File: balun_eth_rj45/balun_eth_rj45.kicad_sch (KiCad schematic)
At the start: 17 parts, among them J1 RJE591885401 CAT6 NO-MAGNETICS, J2 SMA_A, J3 SMA_B, J4 SMA_C, J5 SMA_D, T1 ADT2-1T+, T2 ADT2-1T+, T3 ADT2-1T+, T4 ADT2-1T+

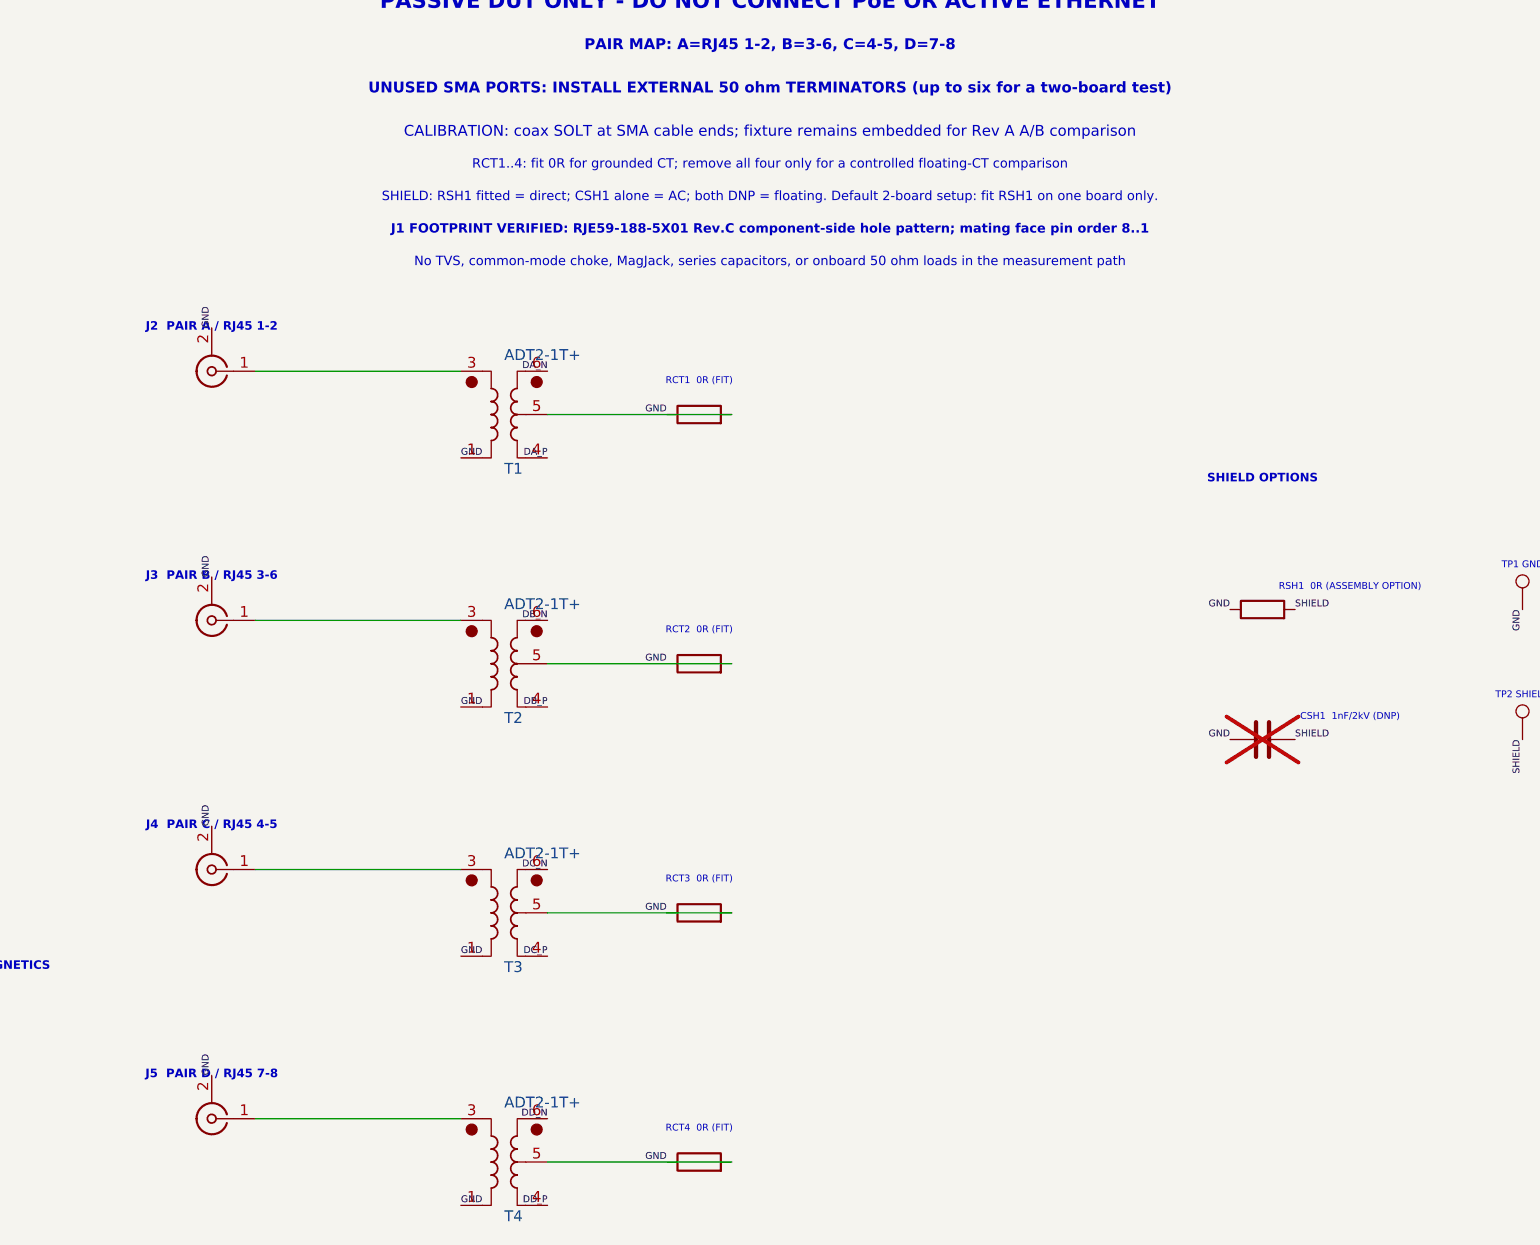
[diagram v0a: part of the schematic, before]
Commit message: feat: finalize slip-ring fixtures and floating CT baseline
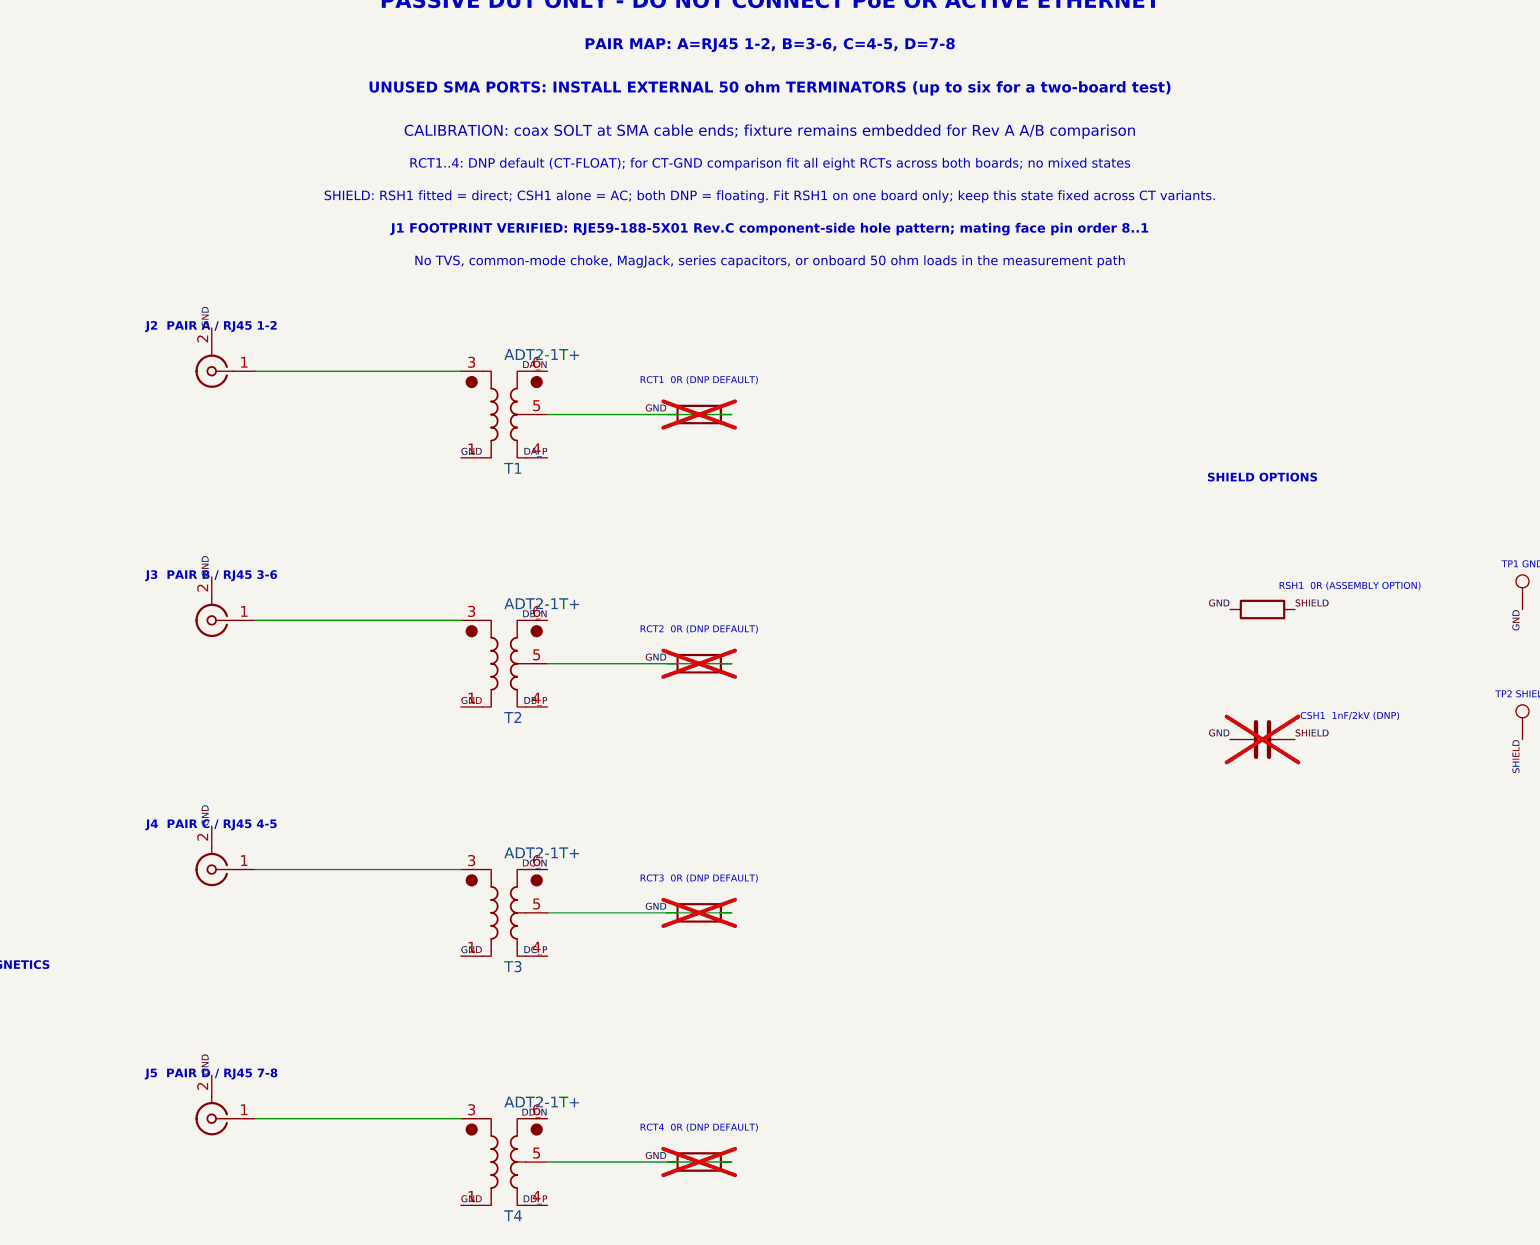
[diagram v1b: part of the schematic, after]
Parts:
- RCT1, RCT2, RCT3, RCT4: Assembly FIT; remove for floating-CT comparison -> DNP DEFAULT; fit all eight only for CT-GND comparison; now not fitted
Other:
- note added: "RCT1 0R (DNP DEFAULT)"
- note added: "RCT1..4: DNP default (CT-FLOAT); for CT-GND comparison fit all eight RCTs across both boards; no mixed states"
- note added: "RCT2 0R (DNP DEFAULT)"
- note added: "RCT3 0R (DNP DEFAULT)"
- note added: "RCT4 0R (DNP DEFAULT)"
- note added: "SHIELD: RSH1 fitted = direct; CSH1 alone = AC; both DNP = floating. Fit RSH1 on one board only; keep this state fixed across CT variants."
- note removed: "RCT1 0R (FIT)"
- note removed: "RCT1..4: fit 0R for grounded CT; remove all four only for a controlled floating-CT comparison"
- note removed: "RCT2 0R (FIT)"
- note removed: "RCT3 0R (FIT)"
- note removed: "RCT4 0R (FIT)"
- note removed: "SHIELD: RSH1 fitted = direct; CSH1 alone = AC; both DNP = floating. Default 2-board setup: fit RSH1 on one board only."
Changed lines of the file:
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@@
 		(comment 4 "RJ45 footprint verified against RJE59-188-5X01 Rev.C component-side drawing.")
 	)
-	(text "RCT3  0R (FIT)"
+	(text "RCT3  0R (DNP DEFAULT)"
 		(exclude_from_sim no)
 		(at 139.7 127 0)
@@
 		)
 	)
-	(text "RCT4  0R (FIT)"
+	(text "RCT4  0R (DNP DEFAULT)"
 		(exclude_from_sim no)
 		(at 139.7 156.21 0)
@@
 		)
 	)
-	(text "RCT1  0R (FIT)"
+	(text "RCT1  0R (DNP DEFAULT)"
 		(exclude_from_sim no)
 		(at 139.7 68.58 0)
@@
 		)
 	)
-	(text "SHIELD: RSH1 fitted = direct; CSH1 alone = AC; both DNP = floating. Default 2-board setup: fit RSH1 on one board only."
+	(text "SHIELD: RSH1 fitted = direct; CSH1 alone = AC; both DNP = floating. Fit RSH1 on one board only; keep this state fixed across CT variants."
 		(exclude_from_sim no)
 		(at 148 46.99 0)
@@
 		)
 	)
-	(text "RCT1..4: fit 0R for grounded CT; remove all four only for a controlled floating-CT comparison"
+	(text "RCT1..4: DNP default (CT-FLOAT); for CT-GND comparison fit all eight RCTs across both boards; no mixed states"
 		(exclude_from_sim no)
 		(at 148 43.18 0)
@@
 		)
 	)
-	(text "RCT2  0R (FIT)"
+	(text "RCT2  0R (DNP DEFAULT)"
 		(exclude_from_sim no)
 		(at 139.7 97.79 0)
@@
 		(in_bom yes)
 		(on_board yes)
-		(in_pos_files yes)
+		(in_pos_files no)
 		(dnp yes)
 		(property "Reference" "CSH1"
@@
 		(in_bom yes)
 		(on_board yes)
-		(in_pos_files yes)
-		(dnp no)
+		(in_pos_files no)
+		(dnp yes)
 		(property "Reference" "RCT1"
 			(at 139.7 72.39 0)
@@
 			)
 		)
-		(property "Assembly" "FIT; remove for floating-CT comparison"
+		(property "Assembly" "DNP DEFAULT; fit all eight only for CT-GND comparison"
 			(at 142.24 77.4699 0)
 			(hide yes)
@@
 		(in_bom yes)
 		(on_board yes)
-		(in_pos_files yes)
-		(dnp no)
+		(in_pos_files no)
+		(dnp yes)
 		(property "Reference" "RCT4"
 			(at 139.7 160.02 0)
@@
 			)
 		)
-		(property "Assembly" "FIT; remove for floating-CT comparison"
+		(property "Assembly" "DNP DEFAULT; fit all eight only for CT-GND comparison"
 			(at 142.24 165.0999 0)
 			(hide yes)
@@
 		(in_bom yes)
 		(on_board yes)
-		(in_pos_files yes)
-		(dnp no)
+		(in_pos_files no)
+		(dnp yes)
 		(property "Reference" "RCT3"
 			(at 139.7 130.81 0)
@@
 			)
 		)
-		(property "Assembly" "FIT; remove for floating-CT comparison"
+		(property "Assembly" "DNP DEFAULT; fit all eight only for CT-GND comparison"
 			(at 142.24 135.8899 0)
 			(hide yes)
@@
 		(in_bom yes)
 		(on_board yes)
-		(in_pos_files yes)
-		(dnp no)
+		(in_pos_files no)
+		(dnp yes)
 		(property "Reference" "RCT2"
 			(at 139.7 101.6 0)
@@
 			)
 		)
-		(property "Assembly" "FIT; remove for floating-CT comparison"
+		(property "Assembly" "DNP DEFAULT; fit all eight only for CT-GND comparison"
 			(at 142.24 106.6799 0)
 			(hide yes)

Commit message: feat: finalize JLC parts and measurement BOM
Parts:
- J1: LCSC Part # (none) -> C5386678
- J2, J3, J4, J5: footprint Connector_Coaxial:SMA_Amphenol_132289_EdgeMount -> balun_eth_rj45:SMA_MyAntenna_A-SMA-KE-16.5A_EdgeMount; Assembly FIT -> FIT; JLC C22467617; Standard PCBA / wave-solder review; LCSC Part # (none) -> C22467617; MPN 132289 -> A-SMA-KE-16.5A; Manufacturer Amphenol RF -> MyAntenna
- RCT1, RCT2, RCT3, RCT4: LCSC Part # (none) -> C17477
- RSH1: Assembly VARIANT; default FIT on one fixture board only -> DNP DEFAULT; hand-fit on Port-1 board only; LCSC Part # (none) -> C17477; now not fitted
- T1, T2, T3, T4: LCSC Part # (none) -> C5223988
- TP1, TP2: LCSC Part # (none) -> C238122
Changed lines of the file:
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@@
+			)
+		)
+		(property "LCSC Part #" "C238122"
+			(at 238.76 100.3299 0)
+			(hide yes)
+			(show_name no)
+			(do_not_autoplace no)
+			(effects
+				(font
+					(size 1.27 1.27)
+				)
 			)
 		)
@@
 			)
 		)
-		(property "Footprint" "Connector_Coaxial:SMA_Amphenol_132289_EdgeMount"
+		(property "Footprint" "balun_eth_rj45:SMA_MyAntenna_A-SMA-KE-16.5A_EdgeMount"
 			(at 82.55 96.52 0)
 			(hide yes)
@@
 			)
 		)
-		(property "Datasheet" "https://www.amphenolrf.com/132289.html"
+		(property "Datasheet" "https://datasheet.lcsc.com/datasheet/pdf/92633ab2cf30de4413e1a152c04a3ed5.pdf?productCode=C22467617"
 			(at 82.55 96.52 0)
 			(hide yes)
@@
 			)
 		)
-		(property "Manufacturer" "Amphenol RF"
+		(property "Manufacturer" "MyAntenna"
 			(at 85.09 101.5999 0)
 			(hide yes)
@@
 			)
 		)
-		(property "MPN" "132289"
+		(property "MPN" "A-SMA-KE-16.5A"
 			(at 85.09 101.5999 0)
 			(hide yes)
@@
 			)
 		)
-		(property "Assembly" "FIT"
+		(property "Assembly" "FIT; JLC C22467617; Standard PCBA / wave-solder review"
 			(at 85.09 101.5999 0)
 			(hide yes)
@@
 				)
 			)
+		)
+		(property "LCSC Part #" "C22467617"
+			(at 0 0 0)
+			(hide yes)
+			(show_name no)
+			(do_not_autoplace no)
+			(effects (font (size 1.27 1.27)))
 		)
 		(pin "1"
@@
 			)
 		)
+		(property "LCSC Part #" "C5223988"
+			(at 119.38 165.0999 0)
+			(hide yes)
+			(show_name no)
+			(do_not_autoplace no)
+			(effects
+				(font
+					(size 1.27 1.27)
+				)
+			)
+		)
 		(pin "1"
 		)
@@
 			)
 		)
-		(property "Footprint" "Connector_Coaxial:SMA_Amphenol_132289_EdgeMount"
+		(property "Footprint" "balun_eth_rj45:SMA_MyAntenna_A-SMA-KE-16.5A_EdgeMount"
 			(at 82.55 154.94 0)
 			(hide yes)
@@
 			)
 		)
-		(property "Datasheet" "https://www.amphenolrf.com/132289.html"
+		(property "Datasheet" "https://datasheet.lcsc.com/datasheet/pdf/92633ab2cf30de4413e1a152c04a3ed5.pdf?productCode=C22467617"
 			(at 82.55 154.94 0)
 			(hide yes)
@@
 			)
 		)
-		(property "Manufacturer" "Amphenol RF"
+		(property "Manufacturer" "MyAntenna"
 			(at 85.09 160.0199 0)
 			(hide yes)
@@
 			)
 		)
-		(property "MPN" "132289"
+		(property "MPN" "A-SMA-KE-16.5A"
 			(at 85.09 160.0199 0)
 			(hide yes)
@@
 			)
 		)
-		(property "Assembly" "FIT"
+		(property "Assembly" "FIT; JLC C22467617; Standard PCBA / wave-solder review"
 			(at 85.09 160.0199 0)
 			(hide yes)
@@
 				)
 			)
+		)
+		(property "LCSC Part #" "C22467617"
+			(at 0 0 0)
+			(hide yes)
+			(show_name no)
+			(do_not_autoplace no)
+			(effects (font (size 1.27 1.27)))
 		)
 		(pin "1"
@@
 			)
 		)
-		(property "Footprint" "Connector_Coaxial:SMA_Amphenol_132289_EdgeMount"
+		(property "Footprint" "balun_eth_rj45:SMA_MyAntenna_A-SMA-KE-16.5A_EdgeMount"
 			(at 82.55 67.31 0)
 			(hide yes)
@@
 			)
 		)
-		(property "Datasheet" "https://www.amphenolrf.com/132289.html"
+		(property "Datasheet" "https://datasheet.lcsc.com/datasheet/pdf/92633ab2cf30de4413e1a152c04a3ed5.pdf?productCode=C22467617"
 			(at 82.55 67.31 0)
 			(hide yes)
@@
 			)
 		)
-		(property "Manufacturer" "Amphenol RF"
+		(property "Manufacturer" "MyAntenna"
 			(at 85.09 72.3899 0)
 			(hide yes)
@@
 			)
 		)
-		(property "MPN" "132289"
+		(property "MPN" "A-SMA-KE-16.5A"
 			(at 85.09 72.3899 0)
 			(hide yes)
@@
 			)
 		)
-		(property "Assembly" "FIT"
+		(property "Assembly" "FIT; JLC C22467617; Standard PCBA / wave-solder review"
 			(at 85.09 72.3899 0)
 			(hide yes)
@@
 				)
 			)
+		)
+		(property "LCSC Part #" "C22467617"
+			(at 0 0 0)
+			(hide yes)
+			(show_name no)
+			(do_not_autoplace no)
+			(effects (font (size 1.27 1.27)))
 		)
 		(pin "1"
@@
 			)
 		)
+		(property "LCSC Part #" "C238122"
+			(at 238.76 115.5699 0)
+			(hide yes)
+			(show_name no)
+			(do_not_autoplace no)
+			(effects
+				(font
+					(size 1.27 1.27)
+				)
+			)
+		)
 		(pin "1"
 		)
@@
 			)
 		)
+		(property "LCSC Part #" "C17477"
+			(at 142.24 77.4699 0)
+			(hide yes)
+			(show_name no)
+			(do_not_autoplace no)
+			(effects
+				(font
+					(size 1.27 1.27)
+				)
+			)
+		)
 		(pin "1"
 		)
@@
 			)
 		)
-		(property "Footprint" "Connector_Coaxial:SMA_Amphenol_132289_EdgeMount"
+		(property "Footprint" "balun_eth_rj45:SMA_MyAntenna_A-SMA-KE-16.5A_EdgeMount"
 			(at 82.55 125.73 0)
 			(hide yes)
@@
 			)
 		)
-		(property "Datasheet" "https://www.amphenolrf.com/132289.html"
+		(property "Datasheet" "https://datasheet.lcsc.com/datasheet/pdf/92633ab2cf30de4413e1a152c04a3ed5.pdf?productCode=C22467617"
 			(at 82.55 125.73 0)
 			(hide yes)
@@
 			)
 		)
-		(property "Manufacturer" "Amphenol RF"
+		(property "Manufacturer" "MyAntenna"
 			(at 85.09 130.8099 0)
 			(hide yes)
@@
 			)
 		)
-		(property "MPN" "132289"
+		(property "MPN" "A-SMA-KE-16.5A"
 			(at 85.09 130.8099 0)
 			(hide yes)
@@
 			)
 		)
-		(property "Assembly" "FIT"
+		(property "Assembly" "FIT; JLC C22467617; Standard PCBA / wave-solder review"
 			(at 85.09 130.8099 0)
 			(hide yes)
@@
 				)
 			)
+		)
+		(property "LCSC Part #" "C22467617"
+			(at 0 0 0)
+			(hide yes)
+			(show_name no)
+			(do_not_autoplace no)
+			(effects (font (size 1.27 1.27)))
 		)
 		(pin "1"
@@
 			)
 		)
+		(property "LCSC Part #" "C5386678"
+			(at 45.72 121.9199 0)
+			(hide yes)
+			(show_name no)
+			(do_not_autoplace no)
+			(effects
+				(font
+					(size 1.27 1.27)
+				)
+			)
+		)
 		(pin "1"
 		)
@@
 			)
 		)
+		(property "LCSC Part #" "C17477"
+			(at 142.24 165.0999 0)
+			(hide yes)
+			(show_name no)
+			(do_not_autoplace no)
+			(effects
+				(font
+					(size 1.27 1.27)
+				)
+			)
+		)
 		(pin "1"
 		)
@@
 			)
 		)
+		(property "LCSC Part #" "C5223988"
+			(at 119.38 77.4699 0)
+			(hide yes)
+			(show_name no)
+			(do_not_autoplace no)
+			(effects
+				(font
+					(size 1.27 1.27)
+				)
+			)
+		)
 		(pin "1"
 		)
@@
 			)
 		)
+		(property "LCSC Part #" "C17477"
+			(at 142.24 135.8899 0)
+			(hide yes)
+			(show_name no)
+			(do_not_autoplace no)
+			(effects
+				(font
+					(size 1.27 1.27)
+				)
+			)
+		)
 		(pin "1"
 		)
@@
 			)
 		)
+		(property "LCSC Part #" "C5223988"
+			(at 119.38 106.6799 0)
+			(hide yes)
+			(show_name no)
+			(do_not_autoplace no)
+			(effects
+				(font
+					(size 1.27 1.27)
+				)
+			)
+		)
 		(pin "1"
 		)
@@
 			)
 		)
+		(property "LCSC Part #" "C5223988"
+			(at 119.38 135.8899 0)
+			(hide yes)
+			(show_name no)
+			(do_not_autoplace no)
+			(effects
+				(font
+					(size 1.27 1.27)
+				)
+			)
+		)
 		(pin "1"
 		)
@@
 		(in_bom yes)
 		(on_board yes)
-		(in_pos_files yes)
-		(dnp no)
+		(in_pos_files no)
+		(dnp yes)
 		(property "Reference" "RSH1"
 			(at 205.74 95.25 0)
@@
 			)
 		)
-		(property "Assembly" "VARIANT; default FIT on one fixture board only"
+		(property "Assembly" "DNP DEFAULT; hand-fit on Port-1 board only"
 			(at 208.28 100.3299 0)
 			(hide yes)
@@
 				)
 			)
+		)
+		(property "LCSC Part #" "C17477"
+			(at 0 0 0)
+			(hide yes)
+			(show_name no)
+			(do_not_autoplace no)
+			(effects (font (size 1.27 1.27)))
 		)
 		(pin "1"
@@
 			(at 142.24 106.6799 0)
 			(hide yes)
+			(show_name no)
+			(do_not_autoplace no)
+			(effects
+				(font
+					(size 1.27 1.27)
+				)
+			)
+		)
+		(property "LCSC Part #" "C17477"
+			(at 142.24 106.6799 0)
+			(hide yes)
